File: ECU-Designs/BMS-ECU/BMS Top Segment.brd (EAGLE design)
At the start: 127 x 110 mm, 90 parts, among them Q10 P-CHANNEL_MOSFET_DMP3099L-7, Q11 P-CHANNEL_MOSFET_DMP3099L-7, Q12 P-CHANNEL_MOSFET_DMP3099L-7, Q13 NPN_BCP56T1, Q3 P-CHANNEL_MOSFET_DMP3099L-7, Q4 P-CHANNEL_MOSFET_DMP3099L-7, Q5 P-CHANNEL_MOSFET_DMP3099L-7, Q6 P-CHANNEL_MOSFET_DMP3099L-7, Q8 P-CHANNEL_MOSFET_DMP3099L-7, Q9 P-CHANNEL_MOSFET_DMP3099L-7

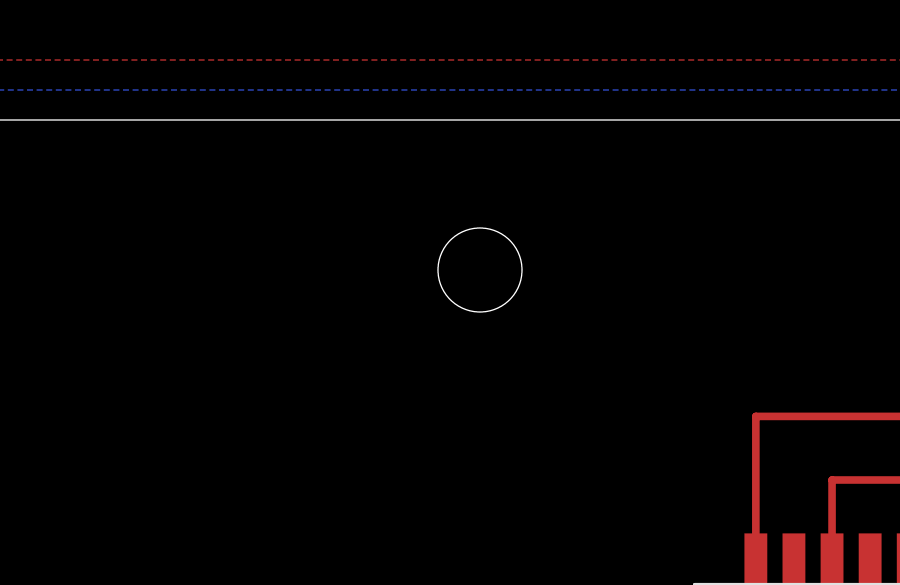
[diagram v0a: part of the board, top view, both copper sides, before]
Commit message: Added mounting holes to BMS segment boards
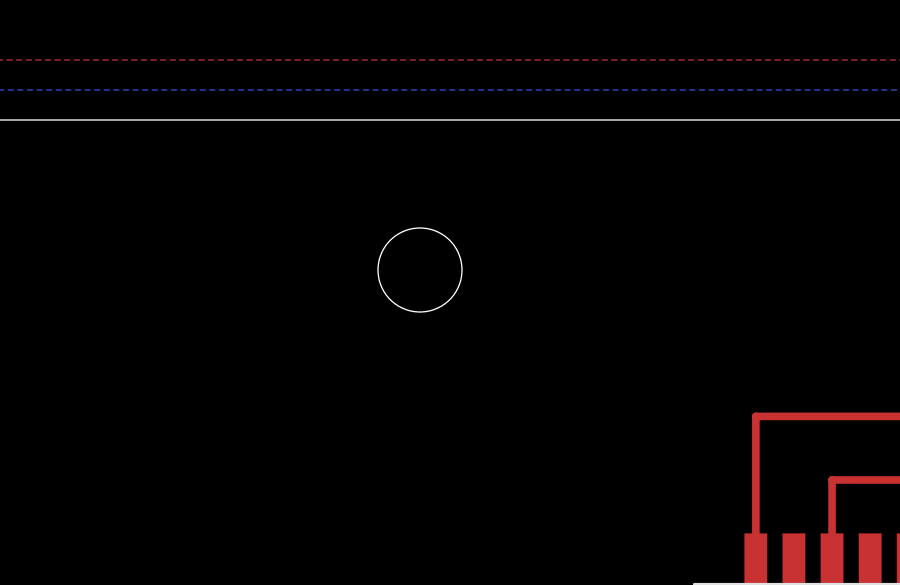
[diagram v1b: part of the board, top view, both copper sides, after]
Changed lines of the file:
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@@
 <hole x="100.5" y="5" drill="2.8"/>
 <hole x="25.5" y="5" drill="2.8"/>
-<hole x="92.5" y="105" drill="2.8"/>
+<hole x="90.5" y="105" drill="2.8"/>
 <hole x="15.5" y="105" drill="2.8"/>
 <polygon width="0.4064" layer="21">
